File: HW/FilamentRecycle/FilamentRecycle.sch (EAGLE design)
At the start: 26 parts, among them CON5 MOLEX-53261-0671, IC1 ATMEGA48A-AU, IC7 FT232RL, Q1 16MHz, Q2 BC847ALT1SMD, Q3 BC847ALT1SMD, X6 PN61729-S

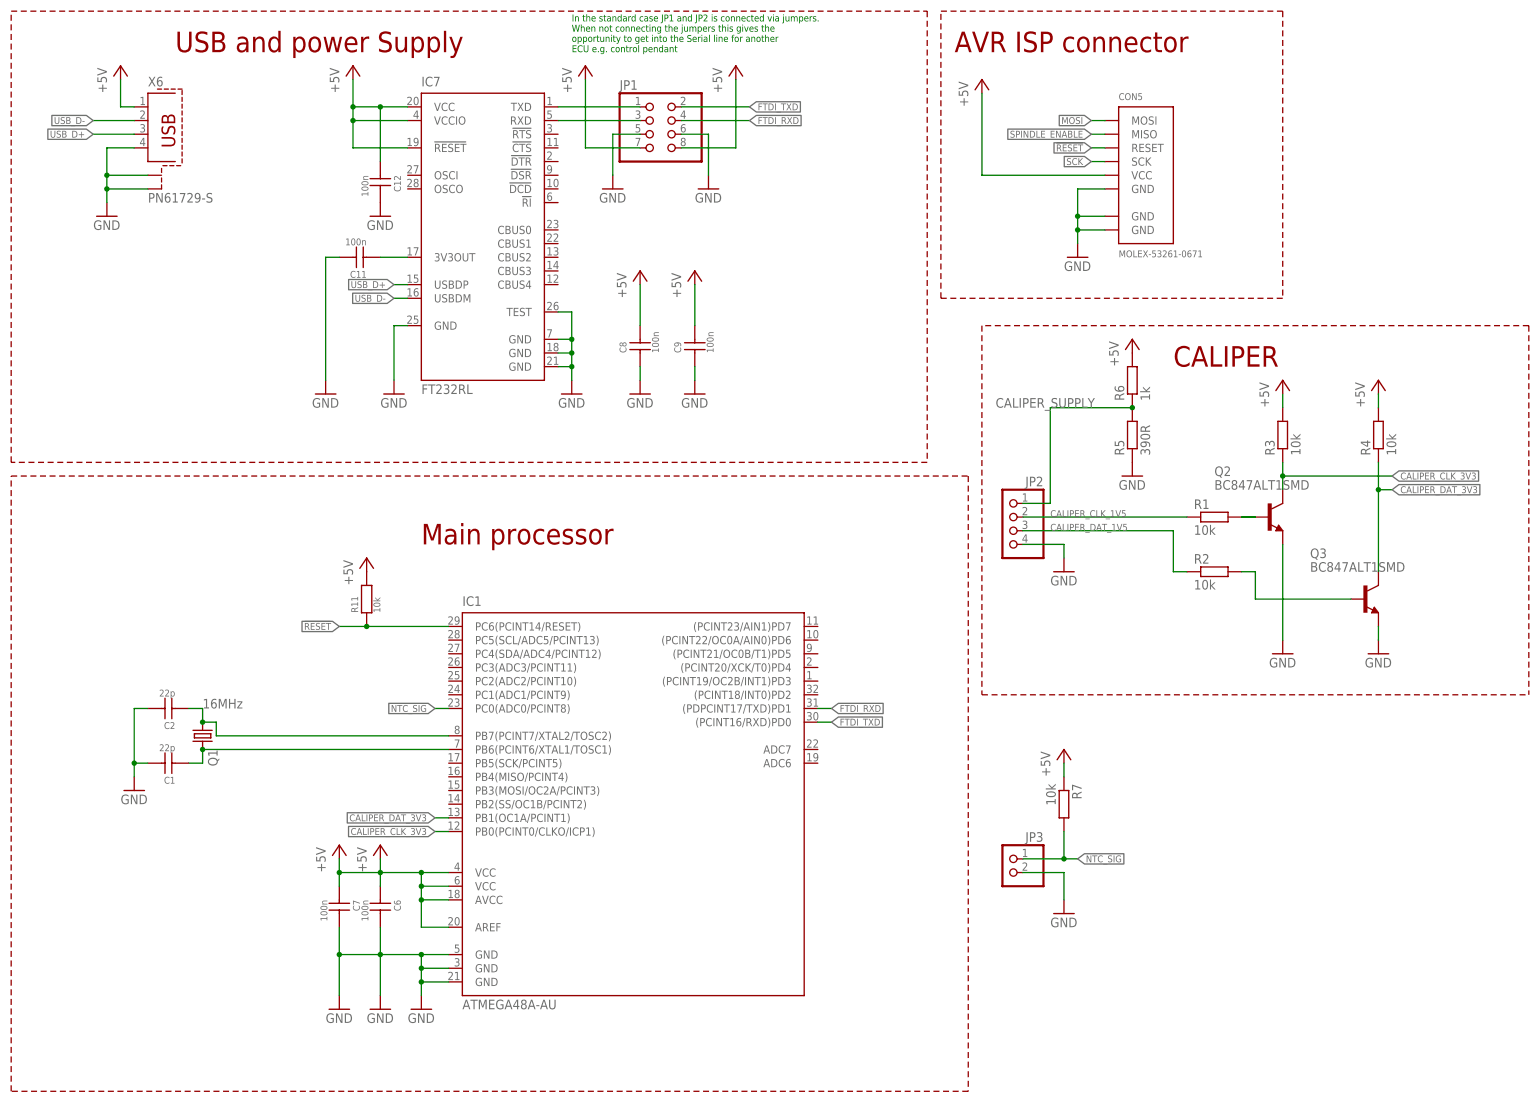
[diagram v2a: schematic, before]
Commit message: Temperatur reading working with NTC3950 thermistor
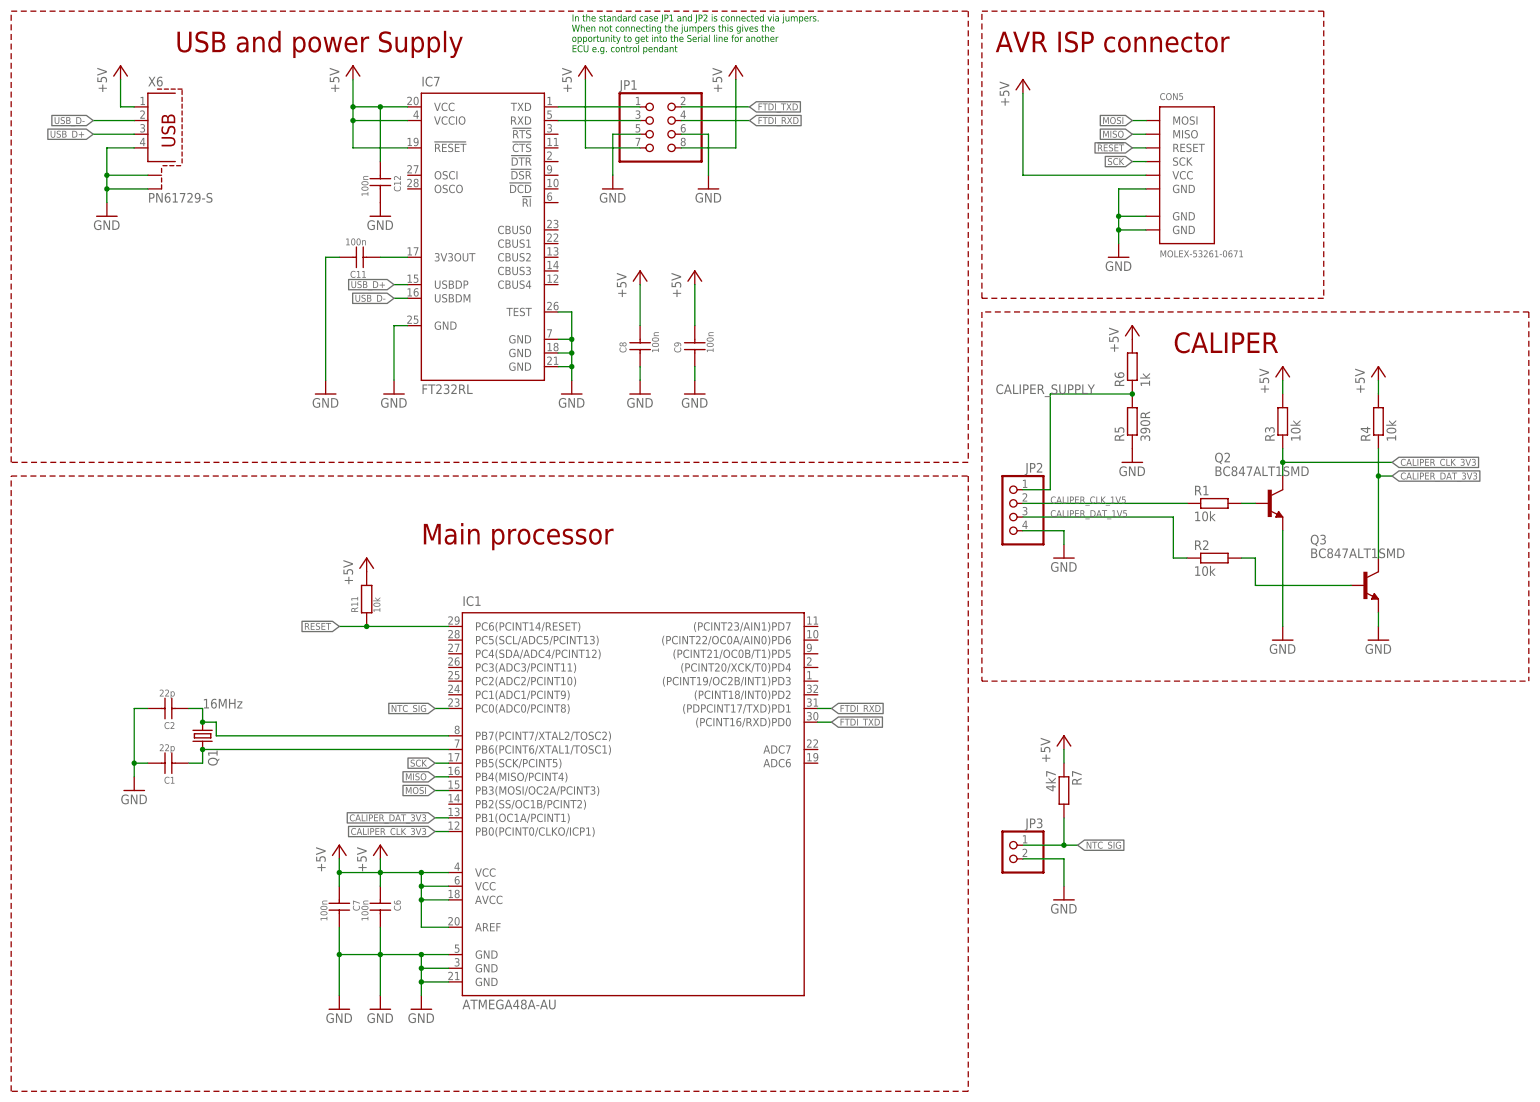
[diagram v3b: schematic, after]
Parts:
- R7: value 10k -> 4k7
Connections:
- removed net SPINDLE_ENABLE: CON5.MISO
- new net MISO: CON5.MISO, IC1.PB4(MISO/PCINT4)
- net MOSI: now also IC1.PB3(MOSI/OC2A/PCINT3)
- net SCK: now also IC1.PB5(SCK/PCINT5)
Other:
- moved on the sheet: CON5, JP2, JP3, Q2, Q3, R1, R2, R3, R4, R5, R6, R7

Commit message: Schematic and board work
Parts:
- added IC2: 74HC595D, 74xx-eu:74HC595D
- added JP4: (no value), pinhead:PINHD-1X2
- added JP5, JP6: (no value), pinhead:PINHD-2X3
- added JP7, JP8: (no value), pinhead:PINHD-1X4
- added R10, R13, R15, R17, R19, R21, R23, R8: 50k, rcl:R-EU_R0603
- added R12, R14, R16, R18, R20, R22, R24, R25, R28, R9: 100k, rcl:R-EU_R0603
- added R26, R27: 10k, rcl:R-EU_R0603
- added S1: (no value), switch-omron:10-XX
- added U$14, U$7: A4988BREAKOUT, RepRapjr:A4988BREAKOUT
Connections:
- new net !MOT_SPINDLE_EN: R26.2, U$7.EN
- new net !MOT_WINDING_EN: R27.2, U$14.EN
- new net +12V: U$14.VMOT, U$7.VMOT
- new net DAC_CLK: IC1.PC4(SDA/ADC4/PCINT12), IC2A.SCK
- new net DAC_MISO: IC1.PC2(ADC2/PCINT10), IC2A.G
- new net DAC_MOSI: IC1.PC1(ADC1/PCINT9), IC2A.SER
- new net DAC_SS: IC1.PC3(ADC3/PCINT11), IC2A.RCK
- new net MOT_SPINDLE_DIR: U$7.DIR
- new net MOT_SPINDLE_STEP: U$7.STEP
- new net MOT_WINDING_DIR: U$14.DIR
- new net MOT_WINDING_STEP: U$14.STEP
- new net N$10: R15.2, R17.1, R18.2
- new net N$11: R13.2, R15.1, R16.2
- new net N$12: R10.2, R13.1, R14.2
- new net N$13: R10.1, R12.2, R8.2
- new net N$14: R23.1, R8.1, R9.2
- new net N$15: IC2A.QA, R9.1
- new net N$16: IC2A.QB, R12.1
- new net N$17: IC2A.QC, R14.1
- new net N$18: IC2A.QD, R16.1
- new net N$19: IC2A.QE, R18.1
- new net N$20: IC2A.QF, R20.1
- new net N$21: IC2A.QG, R22.1
- new net N$22: IC2A.QH, R24.1
- new net N$23: JP5.5, U$7.MS3
- new net N$24: U$7.RST, U$7.SLEEP
- new net N$25: JP5.1, R25.1, U$7.MS1
- new net N$26: JP5.3, U$7.MS2
- new net N$27: JP7.1, U$7.2B
- new net N$28: JP7.2, U$7.2A
- new net N$29: JP7.3, U$7.1A
- new net N$3: JP4.1, R21.2, R24.2
- new net N$30: JP7.4, U$7.1B
- new net N$31: U$7.GND@0
- new net N$32: JP6.5, U$14.MS3
- new net N$33: JP6.1, R28.1, U$14.MS1
- new net N$34: JP6.3, U$14.MS2
- new net N$35: JP8.1, U$14.2B
- new net N$36: JP8.2, U$14.2A
- new net N$37: JP8.3, U$14.1A
- new net N$38: JP8.4, U$14.1B
- new net N$39: U$14.RST, U$14.SLEEP
- new net N$4: R19.2, R21.1, R22.2
- new net N$40: U$14.GND@0
- new net N$6: R17.2, R19.1, R20.2
- new net SS: IC1.PB2(SS/OC1B/PCINT2)
- net !RESET: now also S1.S, S1.S1
- net +5V: now also IC2A.SCL, JP5.2, JP5.4, JP5.6, JP6.2, JP6.4, JP6.6, U$14.VDD, U$7.VDD
- net CALIPER_CLK_3V3: now also IC1.ADC7; no longer IC1.PB0(PCINT0/CLKO/ICP1)
- net CALIPER_DAT_3V3: now also IC1.ADC6; no longer IC1.PB1(OC1A/PCINT1)
- net GND: now also JP4.2, R23.2, R25.2, R26.1, R27.1, R28.2, S1.P, U$14.GND@1, U$7.GND@1
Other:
- note added: "Outputs"
- note added: "Processor related stuff"
- note added: "R/2R ladder output"
- note added: "Sensor Inputs"
- note added: "Stepper motor drivers"
- note added: "Thermistor"
- note removed: "In the standard case JP1 and JP2 is connected via jumpers. When not connecting the jumpers this gives the opportunity to get into the Serial line for another ECU e.g. control pendant"

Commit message: R2R ladder output working via HC595 shift register
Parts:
- added C3: 100n, SchlegelAr_Master:C_SMD0603
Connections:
- removed net DAC_CLK: IC1.PC4(SDA/ADC4/PCINT12), IC2A.SCK
- removed net DAC_MISO: IC1.PC2(ADC2/PCINT10), IC2A.G
- removed net DAC_SS: IC1.PC3(ADC3/PCINT11), IC2A.RCK
- new net DAC_RCK: IC1.PC2(ADC2/PCINT10), IC2A.RCK
- new net DAC_SCK: IC1.PC3(ADC3/PCINT11), IC2A.SCK
- net +5V: now also C3.P$2, IC2P.VCC
- net GND: now also C3.P$1, IC2P.GND
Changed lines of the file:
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@@
 <part name="GND25" library="supply1" deviceset="GND" device=""/>
 <part name="GND26" library="supply1" deviceset="GND" device=""/>
+<part name="P+3" library="supply1" deviceset="+5V" device=""/>
+<part name="GND27" library="supply1" deviceset="GND" device=""/>
+<part name="C3" library="SchlegelAr_Master" deviceset="C_SMD" device="0603" value="100n"/>
 </parts>
 <sheets>
@@
 </segment>
 </net>
-<net name="DAC_MISO" class="0">
+<net name="DAC_RCK" class="0">
 <segment>
 <label x="50.8" y="86.36" size="1.27" layer="95" rot="R180" xref="yes"/>
@@
 </segment>
 </net>
-<net name="DAC_CLK" class="0">
-<segment>
-<label x="50.8" y="91.44" size="1.27" layer="95" rot="R180" xref="yes"/>
-<wire x1="58.42" y1="91.44" x2="50.8" y2="91.44" width="0.1524" layer="91"/>
-<pinref part="IC1" gate="G$1" pin="PC4(SDA/ADC4/PCINT12)"/>
-</segment>
-</net>
-<net name="DAC_SS" class="0">
+<net name="DAC_SCK" class="0">
 <segment>
 <label x="50.8" y="88.9" size="1.27" layer="95" rot="R180" xref="yes"/>
@@
 <instance part="GND25" gate="1" x="48.26" y="142.24" rot="R270"/>
 <instance part="GND26" gate="1" x="48.26" y="93.98" rot="R270"/>
+<instance part="IC2" gate="P" x="154.94" y="124.46"/>
+<instance part="P+3" gate="1" x="154.94" y="137.16"/>
+<instance part="GND27" gate="1" x="154.94" y="111.76"/>
+<instance part="C3" gate="G$1" x="149.86" y="121.92" rot="R90"/>
 </instances>
 <busses>
@@
 <pinref part="GND26" gate="1" pin="GND"/>
 <wire x1="53.34" y1="93.98" x2="50.8" y2="93.98" width="0.1524" layer="91"/>
+</segment>
+<segment>
+<pinref part="IC2" gate="P" pin="GND"/>
+<pinref part="GND27" gate="1" pin="GND"/>
+<wire x1="154.94" y1="114.3" x2="154.94" y2="116.84" width="0.1524" layer="91"/>
+<pinref part="C3" gate="G$1" pin="P$1"/>
+<wire x1="149.86" y1="119.38" x2="149.86" y2="116.84" width="0.1524" layer="91"/>
+<wire x1="149.86" y1="116.84" x2="154.94" y2="116.84" width="0.1524" layer="91"/>
+<junction x="154.94" y="116.84"/>
 </segment>
 </net>
@@
 <pinref part="U$22" gate="G$1" pin="+5V"/>
 </segment>
+<segment>
+<pinref part="IC2" gate="P" pin="VCC"/>
+<pinref part="P+3" gate="1" pin="+5V"/>
+<wire x1="154.94" y1="134.62" x2="154.94" y2="132.08" width="0.1524" layer="91"/>
+<pinref part="C3" gate="G$1" pin="P$2"/>
+<wire x1="149.86" y1="127" x2="149.86" y2="132.08" width="0.1524" layer="91"/>
+<wire x1="149.86" y1="132.08" x2="154.94" y2="132.08" width="0.1524" layer="91"/>
+<junction x="154.94" y="132.08"/>
+</segment>
 </net>
 <net name="N$3" class="0">
@@
 </segment>
 </net>
-<net name="DAC_CLK" class="0">
+<net name="DAC_SCK" class="0">
 <segment>
 <pinref part="IC2" gate="A" pin="SCK"/>
@@
 </segment>
 </net>
-<net name="DAC_SS" class="0">
+<net name="DAC_RCK" class="0">
 <segment>
 <pinref part="IC2" gate="A" pin="RCK"/>
@@
 </segment>
 </net>
-<net name="DAC_MISO" class="0">
-<segment>
-<pinref part="IC2" gate="A" pin="G"/>
-<wire x1="162.56" y1="132.08" x2="160.02" y2="132.08" width="0.1524" layer="91"/>
-<label x="160.02" y="132.08" size="1.27" layer="95" rot="R180" xref="yes"/>
-</segment>
-</net>

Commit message: Eagle brd RC1
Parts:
- removed C12, C8: 100n, SchlegelAr_Master:C_SMD0603
- added X1: (no value), con-wago-508:W237-02P
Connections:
- removed net N$31: U$7.GND@0
- removed net N$40: U$14.GND@0
- removed net SS: IC1.PB2(SS/OC1B/PCINT2)
- net +12V: now also X1-1.KL
- net +5V: no longer C12.P$1, C8.P$2
- net GND: now also IC2A.G, U$14.GND@0, U$7.GND@0, X1-2.KL; no longer C12.P$2, C8.P$1
- net MOT_SPINDLE_DIR: now also IC1.(PCINT19/OC2B/INT1)PD3
- net MOT_SPINDLE_STEP: now also IC1.(PCINT18/INT0)PD2
- net MOT_WINDING_DIR: now also IC1.PC5(SCL/ADC5/PCINT13)
- net MOT_WINDING_STEP: now also IC1.PC4(SDA/ADC4/PCINT12)
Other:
- moved on the sheet: IC2, JP4, R10, R12, R13, R14, R15, R16, R17, R18, R19, R20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
